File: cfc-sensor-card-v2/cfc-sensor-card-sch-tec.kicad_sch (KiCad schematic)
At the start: 17 parts, among them Q6 PMV45EN, Q7 DMP3050LVT-7, U14 MP2410A

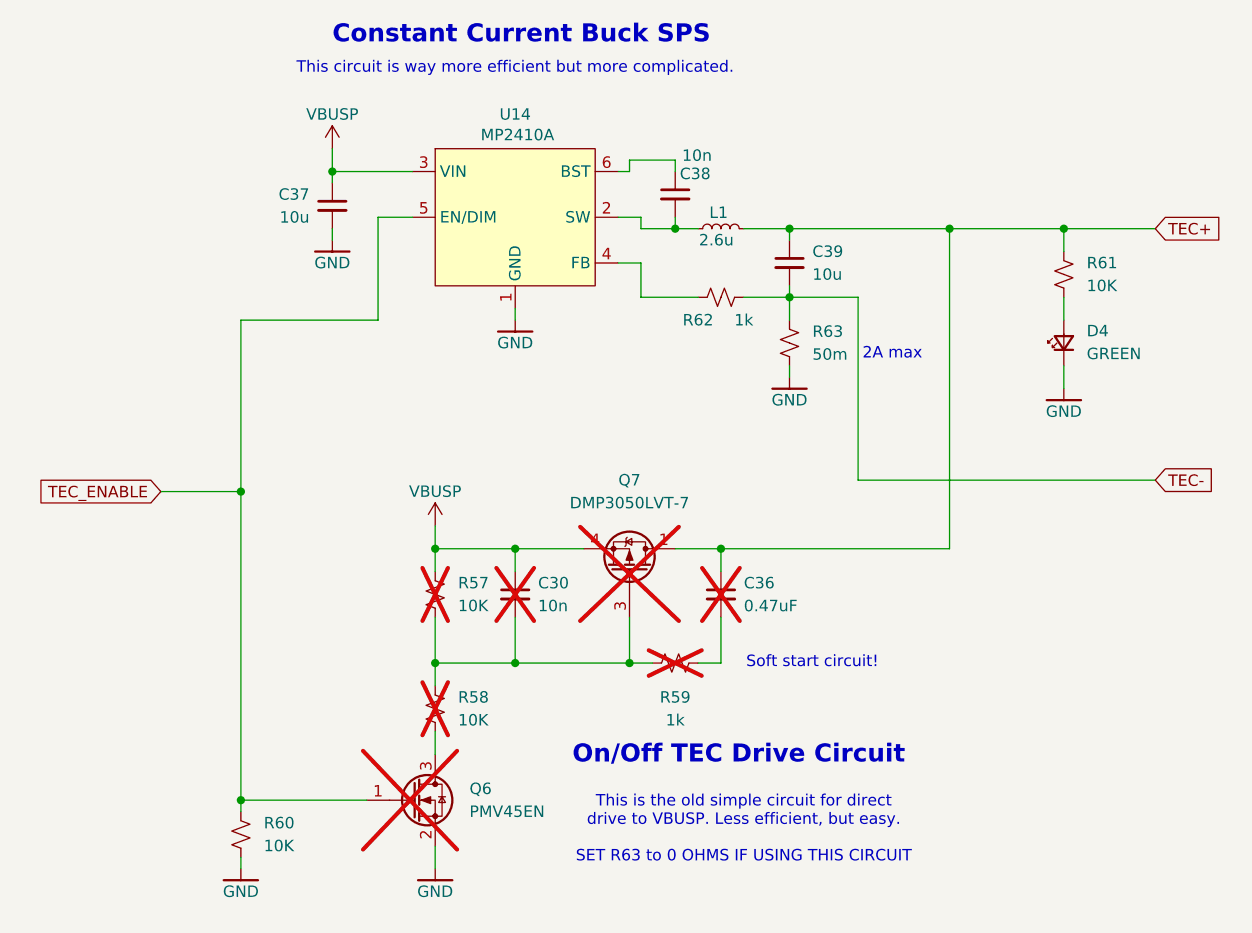
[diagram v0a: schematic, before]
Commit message: Schematic Changes
Made schematic into hierarchy view. Revised OPD to match modern OPD. Removed connectors page. Separated power sequencing and PIRT sensor into 2 pages.
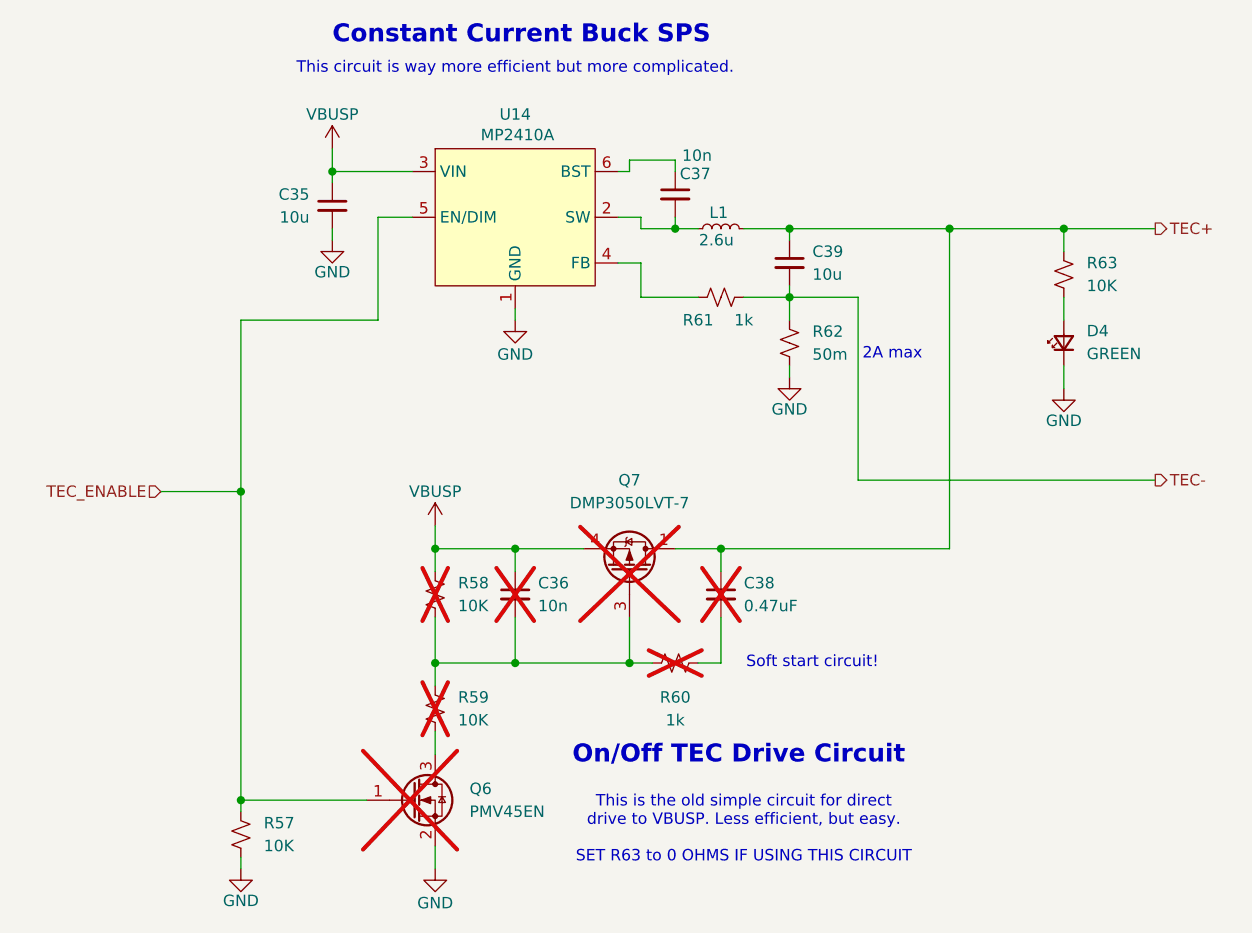
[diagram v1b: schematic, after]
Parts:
- renumbered C37 to C35, C30 to C36, C38 to C37, C36 to C38, R60 to R57, R57 to R58, R58 to R59, R59 to R60, R62 to R61, R63 to R62, R61 to R63

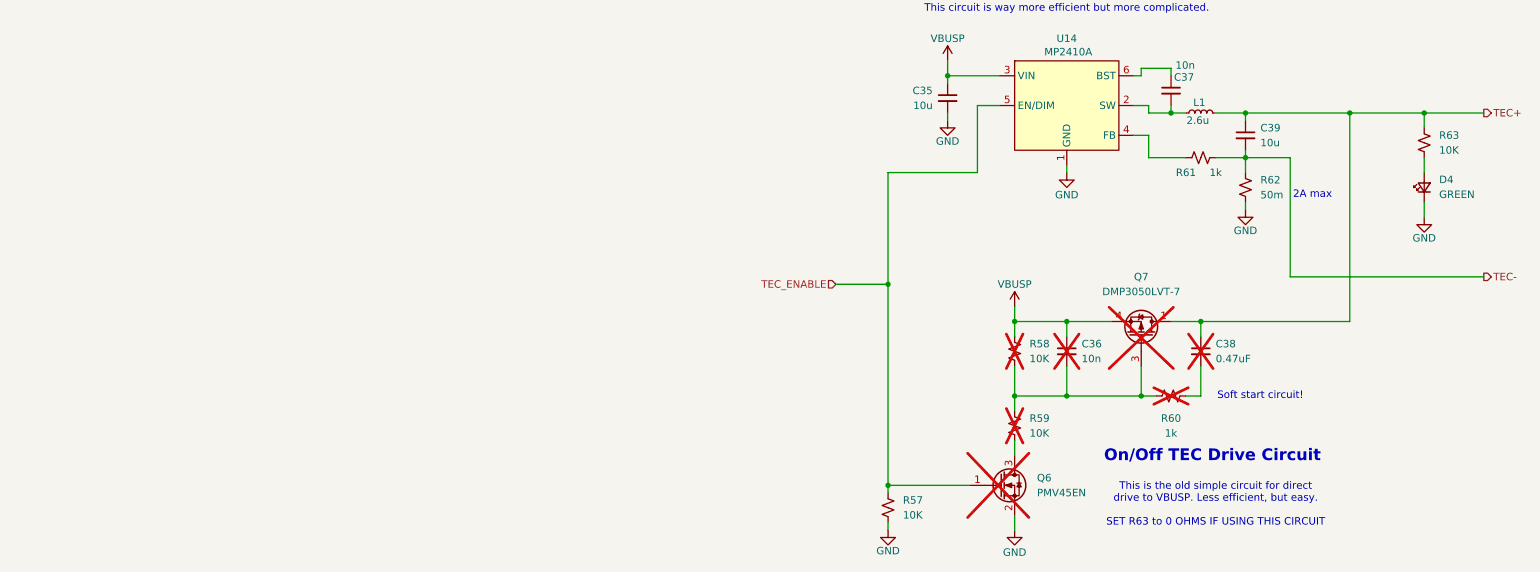
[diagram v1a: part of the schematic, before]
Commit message: Update
Fixed a couple of library issues on testpoints and other misc components. Added Pull up resistors to 8 channel i2c ic
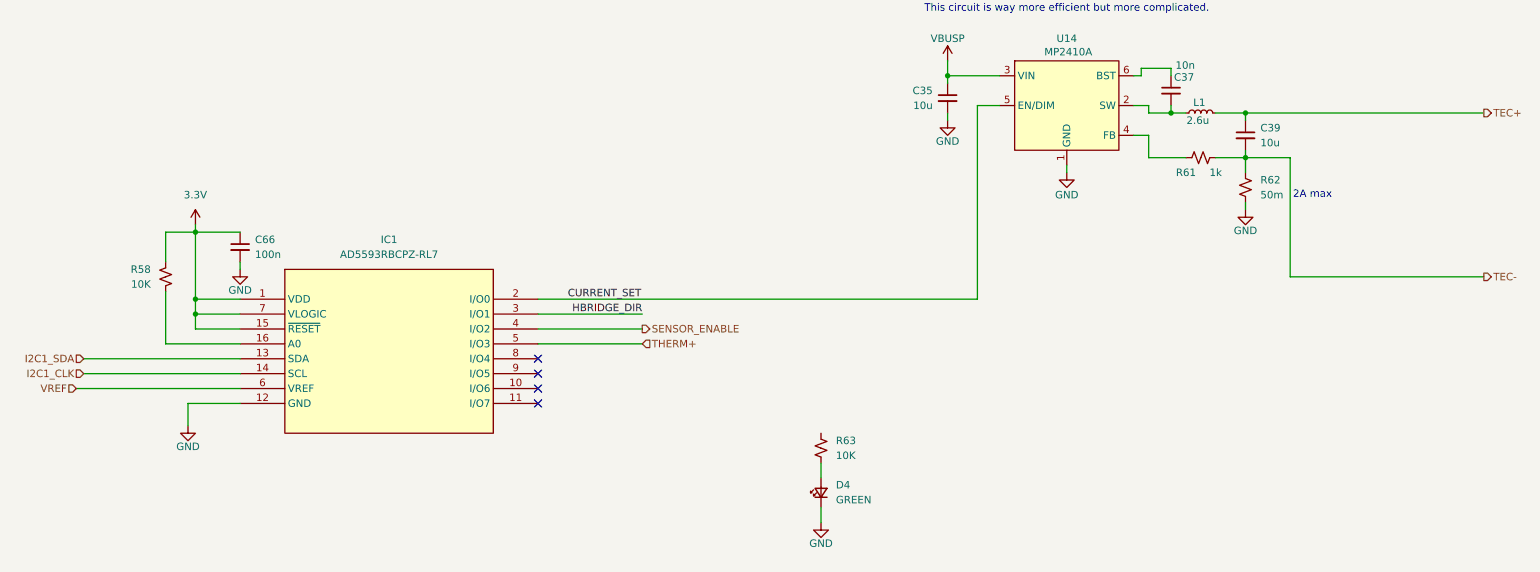
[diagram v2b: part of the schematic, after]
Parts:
- removed C36: 10n, Capacitor_SMD:C_0603_1608Metric_Pad1.08x0.95mm_HandSolder, symbol Device:C_Small
- removed C38: 0.47uF, Capacitor_SMD:C_0603_1608Metric_Pad1.08x0.95mm_HandSolder, symbol Device:C_Small
- removed Q6: PMV45EN, Package_TO_SOT_SMD:SOT-23-3, symbol Transistor_FET:Q_NMOS_GSD
- removed Q7: DMP3050LVT-7, Package_TO_SOT_SMD:TSOT-23-6, symbol oresat-transistors:DMP3050LVT-7
- removed R57, R59: 10K, Resistor_SMD:R_0603_1608Metric_Pad0.98x0.95mm_HandSolder, symbol Device:R_Small_US
- removed R60: 1k, Resistor_SMD:R_0603_1608Metric_Pad0.98x0.95mm_HandSolder, symbol Device:R_Small_US
- added C66: 100n, Capacitor_SMD:C_0603_1608Metric_Pad1.08x0.95mm_HandSolder, symbol Device:C_Small
- added IC1: AD5593RBCPZ-RL7, oresat-ics:16-WFQFN, CSP, symbol oresat-ics:AD5593RBCPZ-RL7
- R58: DIS (none) -> DigiKey; DPN (none) -> RMCF0603FT10K0CT-ND; MFR (none) -> Stackpole Electronics Inc; MPN (none) -> RMCF0603FT10K0; now fitted
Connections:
- net GND: now also C66.2, IC1.12 (GND)
- net TEC+: no longer R63.2
- net VBUSP: no longer R58.1
- net at R58.2: now also IC1.16 (A0)
- net TEC_ENABLE renamed CURRENT_SET
- net CURRENT_SET: now also IC1.2 (I/O0)
- new net 3.3V: C66.1, IC1.1 (VDD), IC1.15 (~{RESET}), IC1.7 (VLOGIC), R58.1
- new net HBRIDGE_DIR: IC1.3 (I/O1)
- new net I2C1_CLK: IC1.14 (SCL)
- new net I2C1_SDA: IC1.13 (SDA)
- new net SENSOR_ENABLE: IC1.4 (I/O2)
- new net THERM+: IC1.5 (I/O3)
- new net VREF: IC1.6 (VREF)
- no-connect marks 0 -> 4
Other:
- note removed: "On/Off TEC Drive Circuit"
- note removed: "SET R63 to 0 OHMS IF USING THIS CIRCUIT"
- note removed: "Soft start circuit!"
- note removed: "This is the old simple circuit for direct drive to VBUSP. Less efficient, but easy."
- moved on the sheet: D4, R63

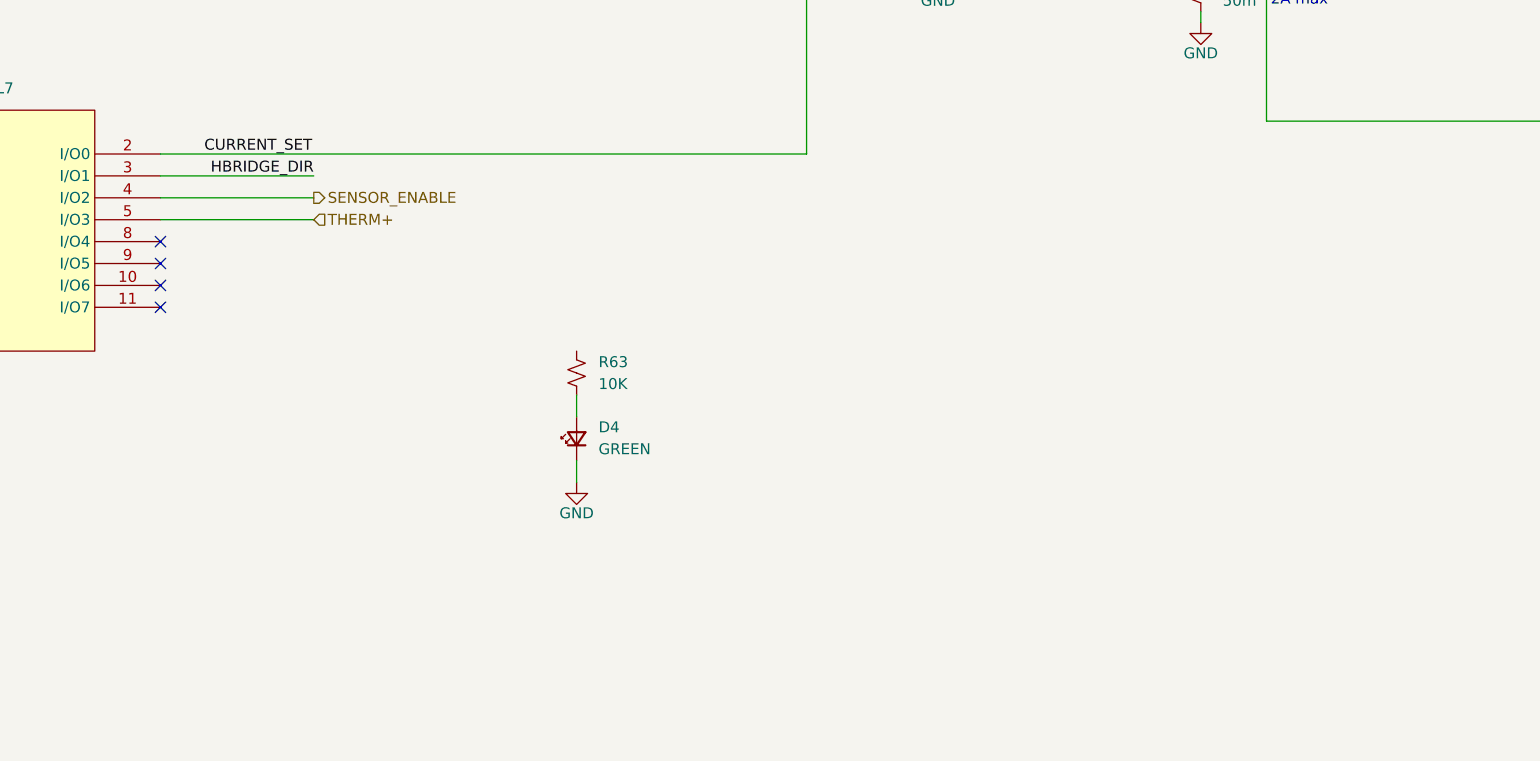
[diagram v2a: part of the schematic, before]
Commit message: Update
Changed passive component footprints to 0603 no silk c. Fixed OPD UART termination resistor on cfc processor card. Added low temp co and tolerance resistor for NTC  thermistor tec voltage divider.
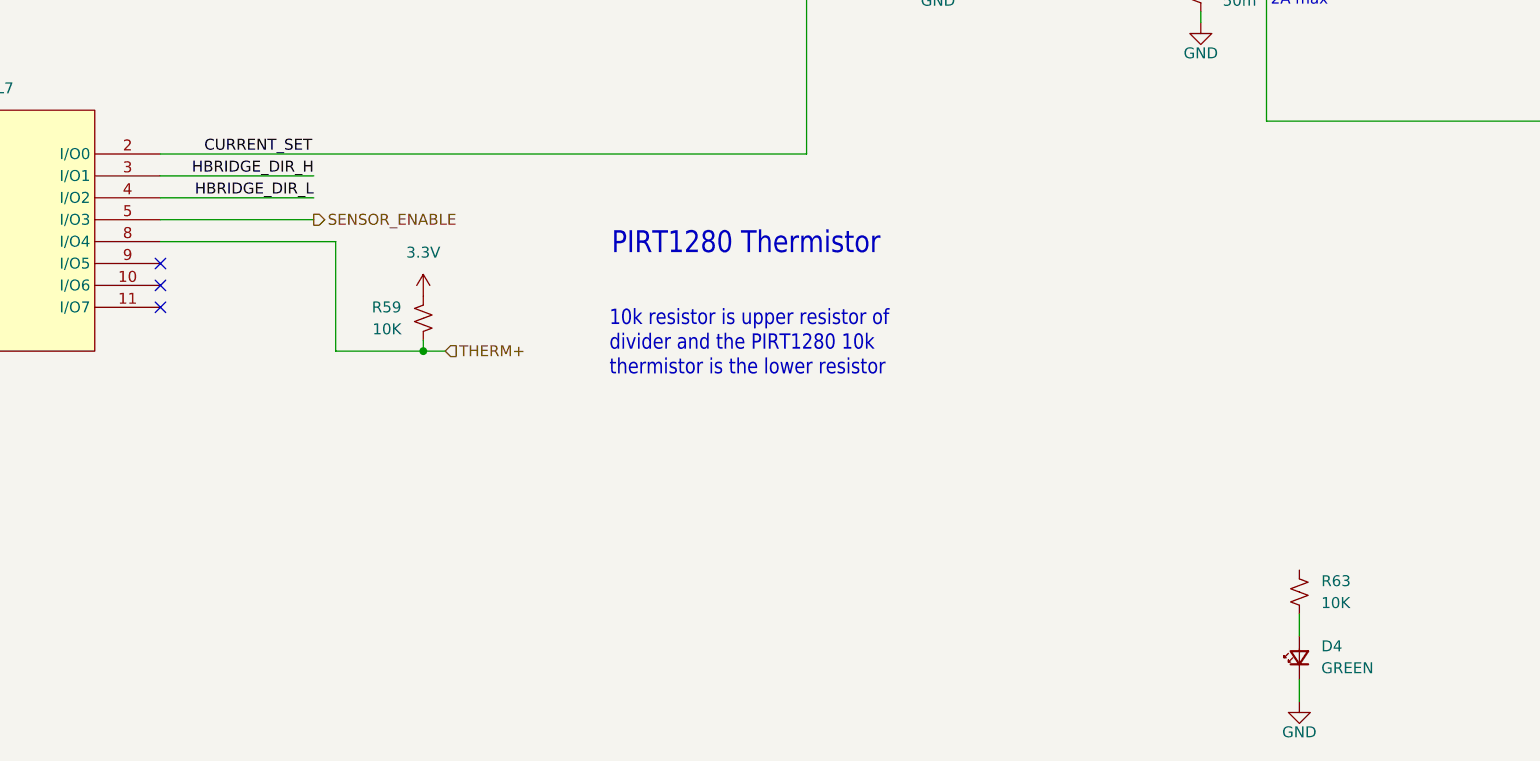
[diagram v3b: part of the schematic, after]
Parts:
- added R59: 10K, oresat-passives:0603-C-NOSILK, symbol Device:R_Small_US
- C35, C39: footprint Capacitor_SMD:C_0805_2012Metric_Pad1.18x1.45mm_HandSolder -> oresat-passives:0805-C-NOSILK
- C37, C66: footprint Capacitor_SMD:C_0603_1608Metric_Pad1.08x0.95mm_HandSolder -> oresat-passives:0603-C-NOSILK
- R58, R61, R63: footprint Resistor_SMD:R_0603_1608Metric_Pad0.98x0.95mm_HandSolder -> oresat-passives:0603-C-NOSILK
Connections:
- net 3.3V: now also R59.1
- net SENSOR_ENABLE: now also IC1.5 (I/O3); no longer IC1.4 (I/O2)
- net THERM+: now also IC1.8 (I/O4), R59.2; no longer IC1.5 (I/O3)
- net HBRIDGE_DIR renamed HBRIDGE_DIR_H
- new net HBRIDGE_DIR_L: IC1.4 (I/O2)
- no-connect marks 4 -> 3
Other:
- note added: "10k resistor is upper resistor of divider and the PIRT1280 10k thermistor is the lower resistor"
- note added: "PIRT1280 Thermistor"
- moved on the sheet: D4, R63

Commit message: Update
Cleaned up library preferences, added voltage controlled constant current note. Added RC filter to therm+ measurement made against the 2.5vref.
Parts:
- added C67, C68: 100n, oresat-passives:0603-C-NOSILK, symbol Device:C_Small
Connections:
- net 3.3V: no longer R59.1
- net GND: now also C67.2, C68.2
- net TEC+: no longer C39.1, L1.2
- net TEC-: no longer C39.2, R61.2, R62.1
- net THERM+: now also IC1.11 (I/O7), C68.1; no longer IC1.8 (I/O4)
- net at R63.2: now also C39.1, L1.2
- net VREF renamed 2.5VREF
- net 2.5VREF: now also R59.1, C67.1
- new net: C39.2, R61.2, R62.1
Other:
- note added: "Scale voltage between .7-1.44v for 0-2A CC output"
- moved on the sheet: C66, D4, IC1, R58, R59, R63

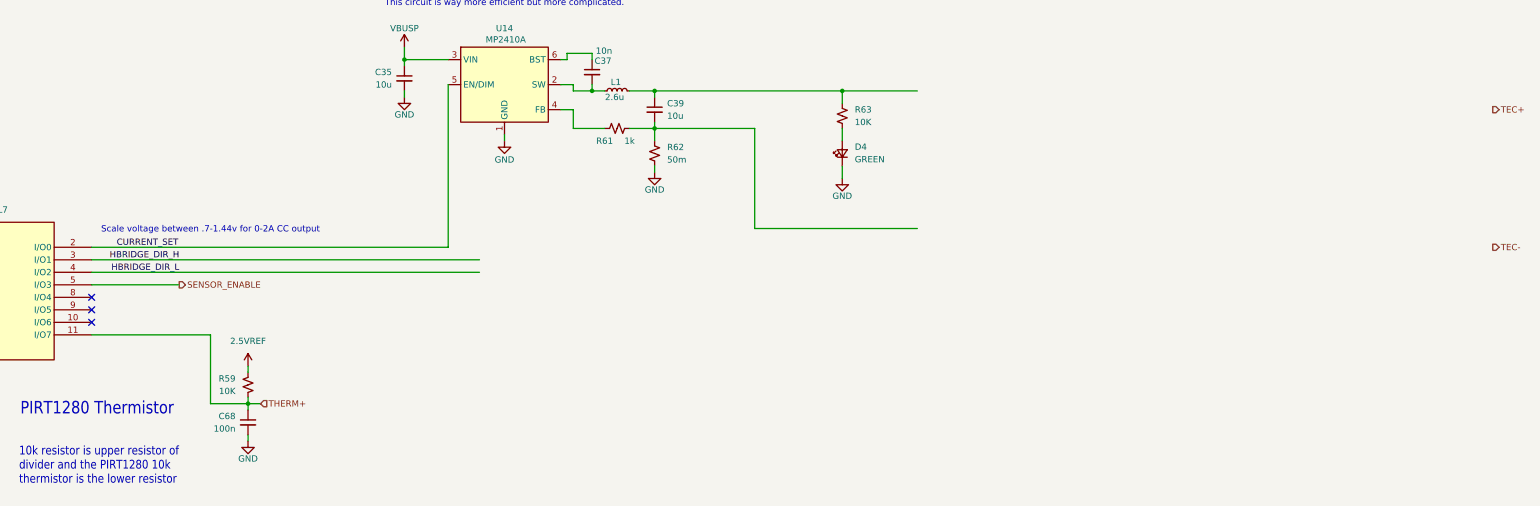
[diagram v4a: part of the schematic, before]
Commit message: Update
Added bidirectional TEC control with DRV8212 IC. Added Sensor enable pin back to processor; in case of i2c hang up octavo can still disable sensor.
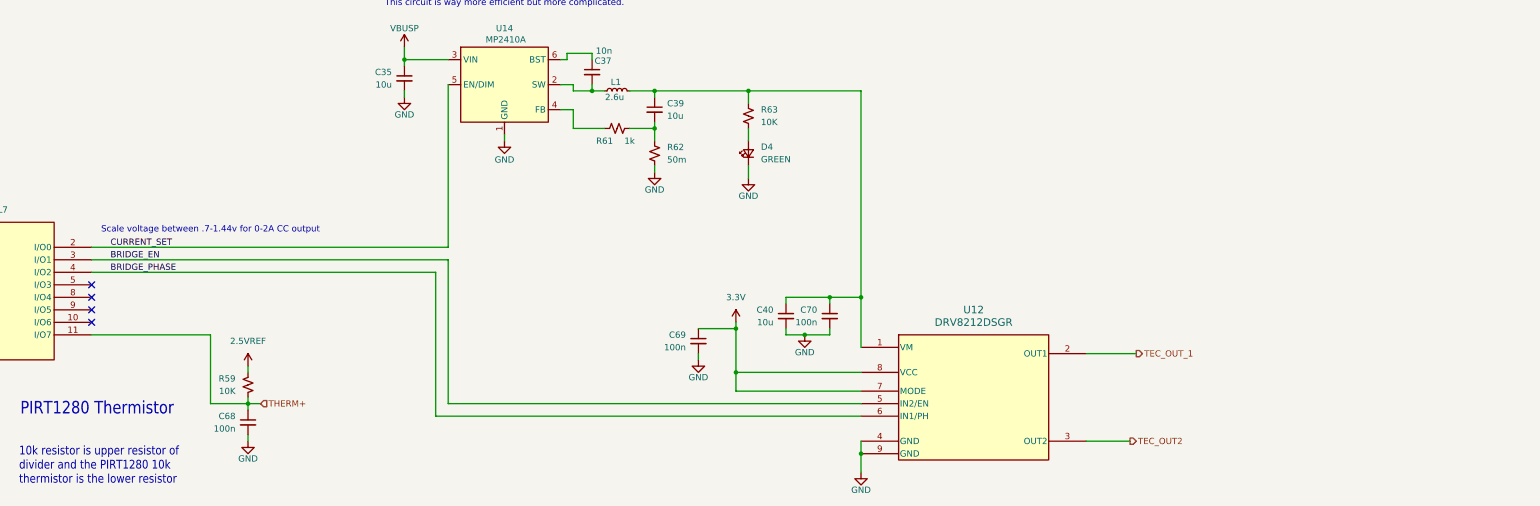
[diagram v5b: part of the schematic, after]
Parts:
- added C40: 10u, oresat-passives:0805-C-NOSILK, symbol Device:C_Small
- added C69, C70: 100n, oresat-passives:0603-C-NOSILK, symbol Device:C_Small
- added U12: DRV8212DSGR, oresat-ics:WSON_212DSGR_TEX, symbol oresat-ics:DRV8212DSGR
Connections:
- net 3.3V: now also C69.1, U12.7 (MODE), U12.8 (VCC)
- net GND: now also C40.2, C69.2, C70.2, U12.4 (GND), U12.9 (GND)
- net at C39.1, L1.2, R63.2: now also C40.1, C70.1, U12.1 (VM)
- net HBRIDGE_DIR_H renamed BRIDGE_EN
- net BRIDGE_EN: now also U12.5 (IN2/EN)
- net HBRIDGE_DIR_L renamed BRIDGE_PHASE
- net BRIDGE_PHASE: now also U12.6 (IN1/PH)
- net SENSOR_ENABLE: no longer names the net of IC1.5 (I/O3)
- new net TEC_OUT2: U12.3 (OUT2)
- new net TEC_OUT_1: U12.2 (OUT1)
- no-connect marks 3 -> 4
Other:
- moved on the sheet: D4, R63
